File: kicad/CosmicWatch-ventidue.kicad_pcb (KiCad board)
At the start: 2 copper layers, 102.5 x 112.5 mm, 115 parts, among them J101 Conn_01x05, J102 Conn_01x07, J103 Conn_01x05, J104 Conn_01x07, J105 Conn_01x05, J106 Conn_01x07, J107 Conn_01x05, J108 Conn_01x07, J109 BMP280, J110 Conn_01x06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

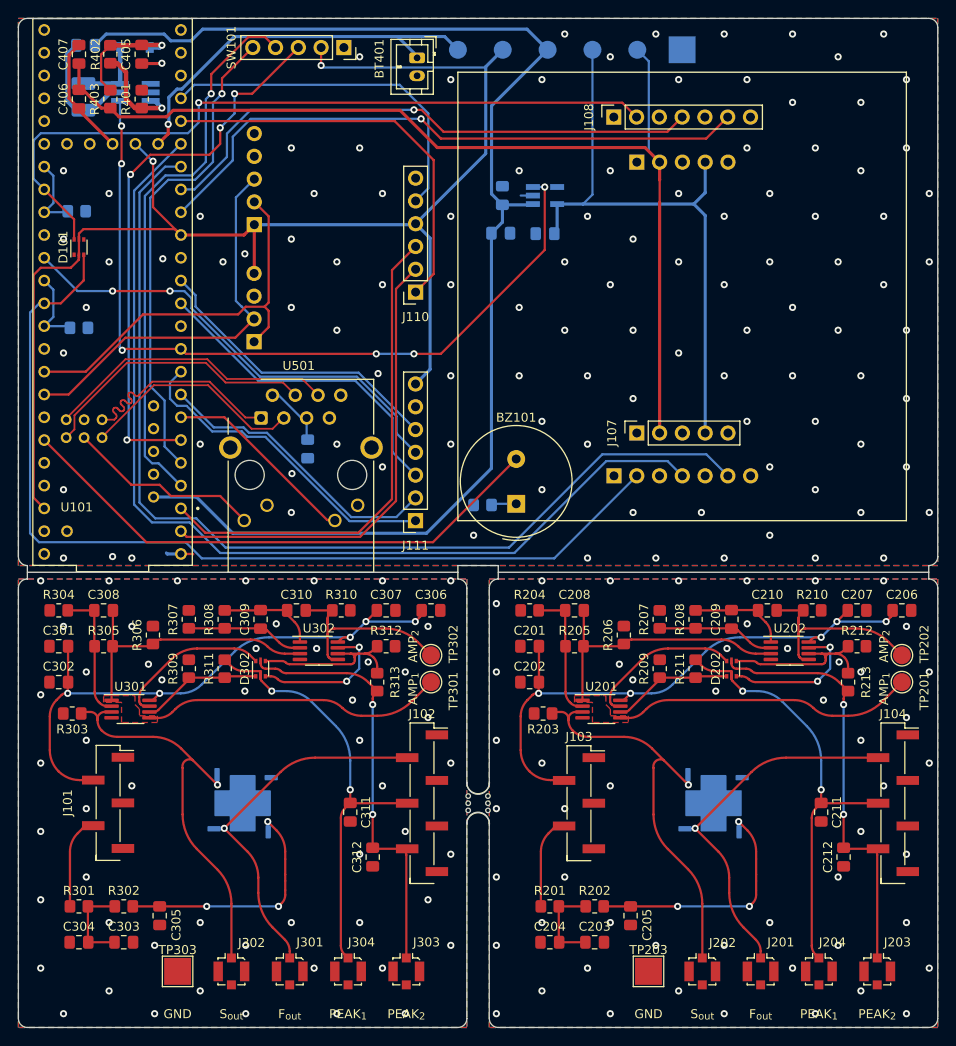
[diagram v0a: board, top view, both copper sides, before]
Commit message: Added gerber files in kicad/plots, both compressed and uncompressed
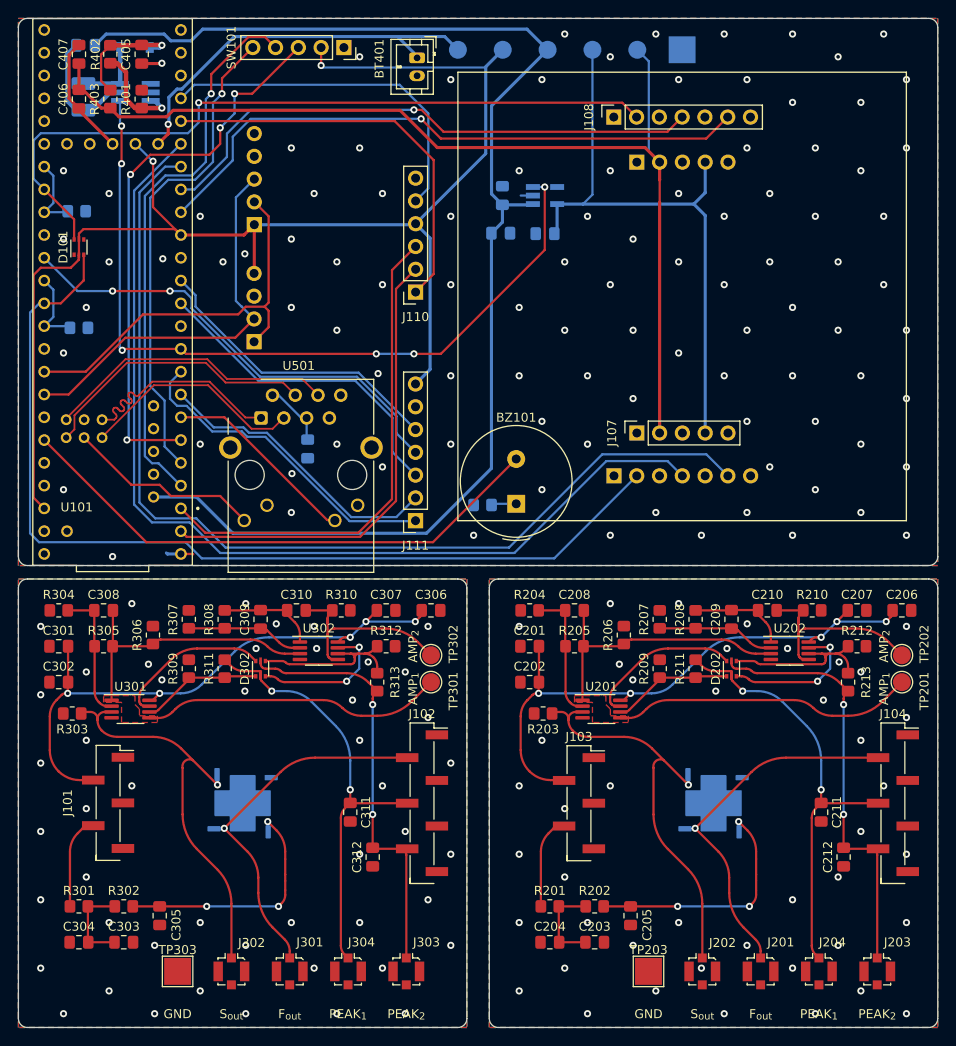
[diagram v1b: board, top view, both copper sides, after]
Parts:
- removed mouse-bite-2.54mm-slot: VAL**, Panelization:mouse-bite-2.54mm-slot
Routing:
- net GND: vias 104 -> 97
- net /Detector PCB 2/GND: vias 52 -> 43
- net /Detector PCB 1/GND: vias 53 -> 48
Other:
- outline, holes or cut-outs redrawn
